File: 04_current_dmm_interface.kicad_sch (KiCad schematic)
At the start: 17 parts, among them J10 POMONA 73099 BLACK, J11 POMONA 73099 RED, J12 POMONA 73099 BLACK, J4 1190370 16POS, J5 691137710006 DMM, J6 POMONA 73099 RED, J8 POMONA 73099 BLACK, J9 POMONA 73099 RED, K13 UD2-5NE, K14 UD2-5NE, K15 UD2-5NE, K16 UD2-5NE

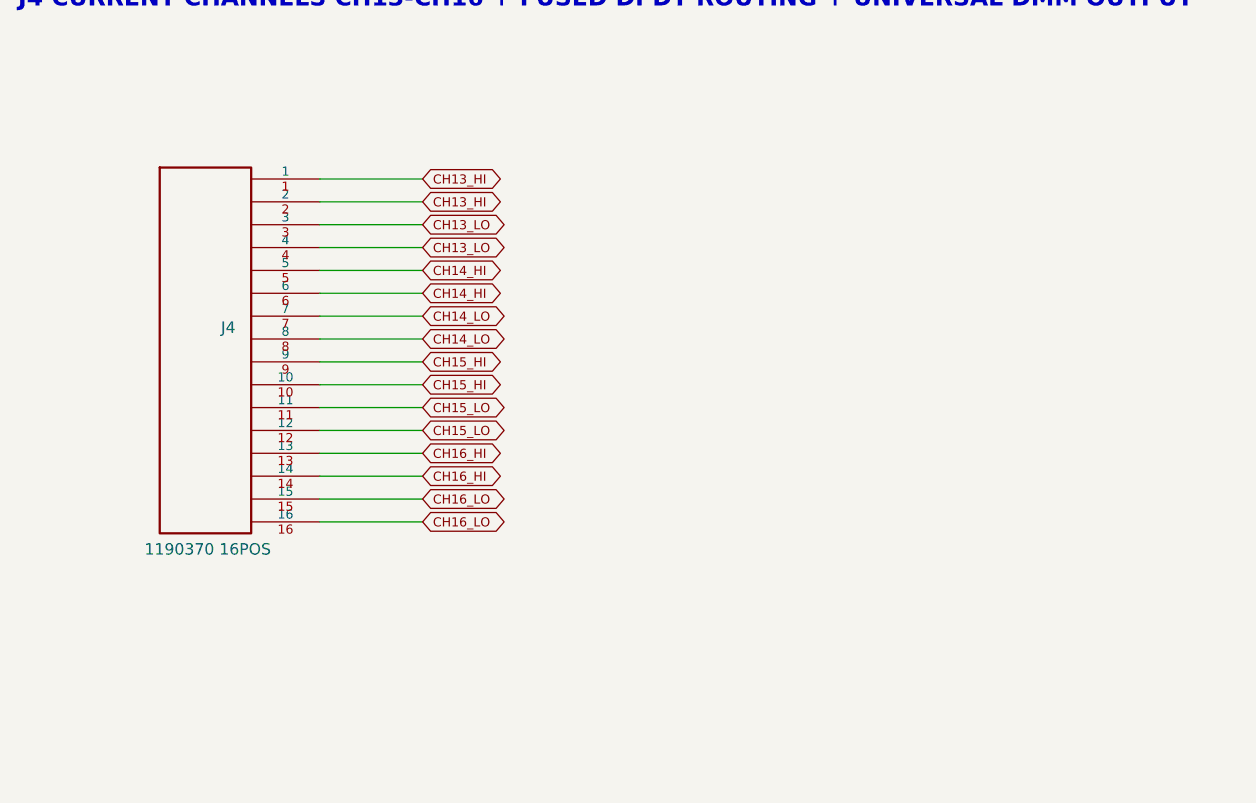
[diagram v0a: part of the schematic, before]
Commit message: Add Phoenix 1190370 connector footprint
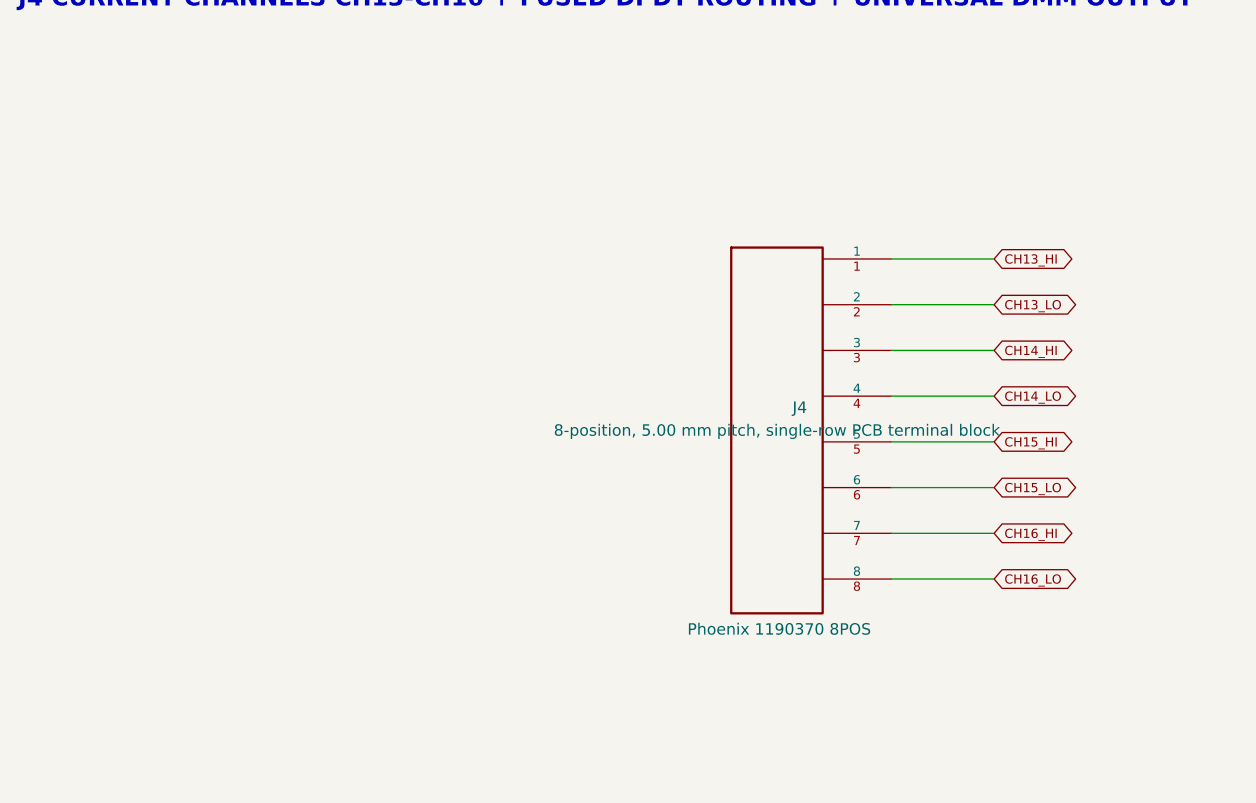
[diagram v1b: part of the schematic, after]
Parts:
- J4: value 1190370 16POS -> Phoenix 1190370 8POS; footprint (none) -> BenchScan_Connectors:Phoenix_1190370_LPTA-2.5-8-5.0; symbol BenchScan_DMMX16-rescue:CONN16 -> BenchScan_DMMX16-rescue:CONN8
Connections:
- net CH13_HI: no longer J4.2
- net CH13_LO: now also J4.2; no longer J4.3, J4.4
- net CH14_HI: now also J4.3; no longer J4.5, J4.6
- net CH14_LO: now also J4.4; no longer J4.7, J4.8
- net CH15_HI: now also J4.5; no longer J4.10, J4.9
- net CH15_LO: now also J4.6; no longer J4.11, J4.12
- net CH16_HI: now also J4.7; no longer J4.13, J4.14
- net CH16_LO: now also J4.8; no longer J4.15, J4.16

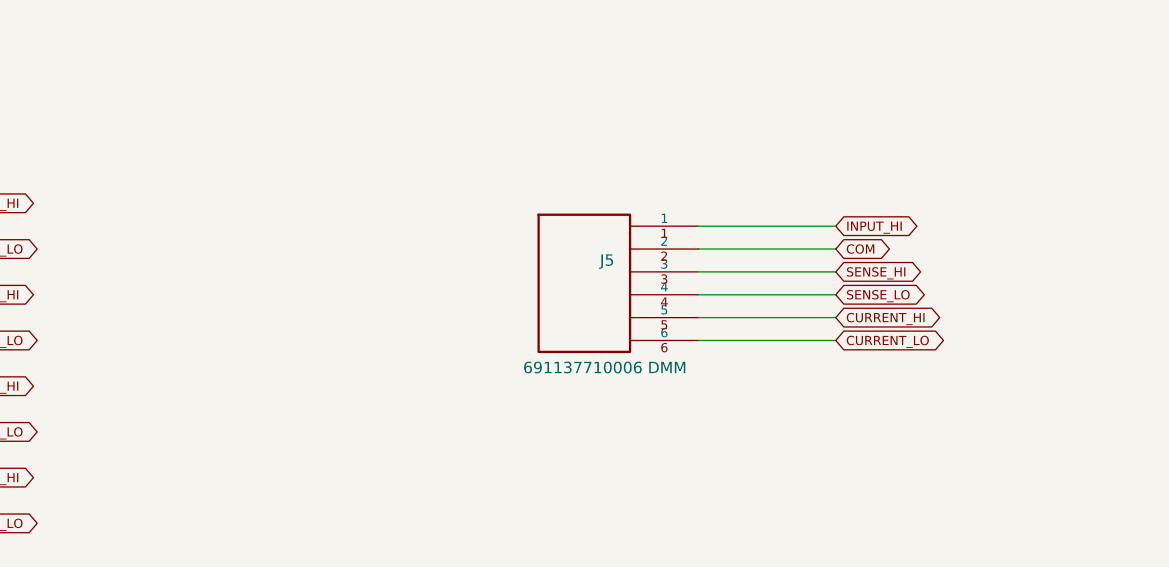
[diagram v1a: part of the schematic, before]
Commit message: Import XIAO and Wurth vendor footprints
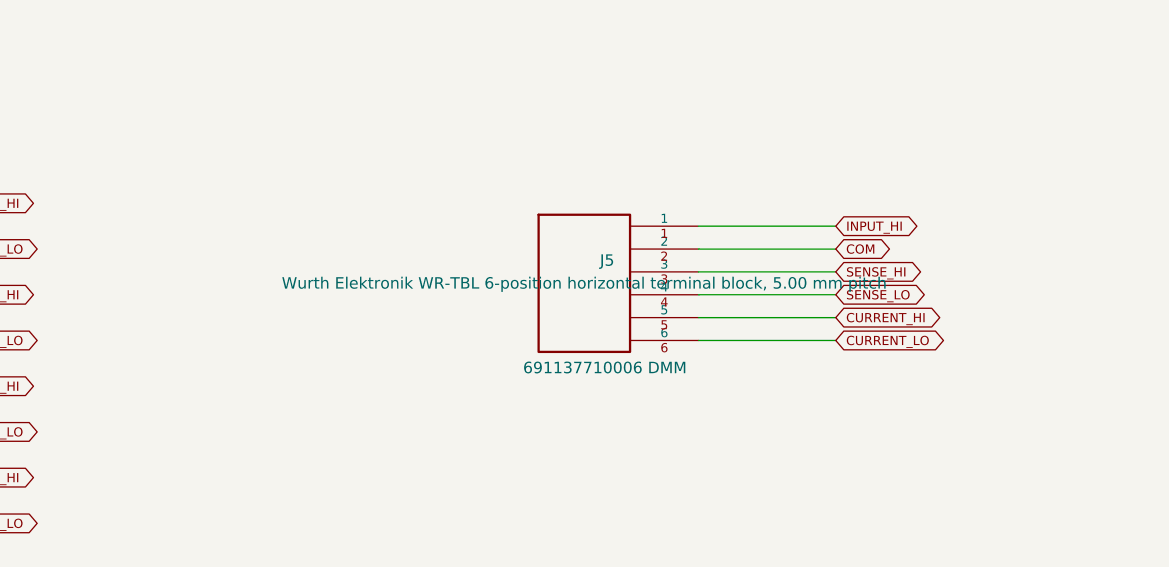
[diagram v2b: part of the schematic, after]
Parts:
- J5: footprint (none) -> Wurth_Connectors:J_Wurth_WR-TBL_691137710006
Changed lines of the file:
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@@
 			)
 		)
-		(property "Footprint" ""
+		(property "Footprint" "Wurth_Connectors:J_Wurth_WR-TBL_691137710006"
 			(at 193.04 54.61 0)
 			(hide yes)
@@
 			)
 		)
-		(property "Datasheet" ""
+		(property "Datasheet" "https://www.we-online.com/components/products/datasheet/691137710006.pdf"
 			(at 193.04 54.61 0)
 			(hide yes)
@@
 			)
 		)
-		(property "Description" ""
+		(property "Description" "Wurth Elektronik WR-TBL 6-position horizontal terminal block, 5.00 mm pitch"
 			(at 193.04 54.61 0)
 			(show_name no)

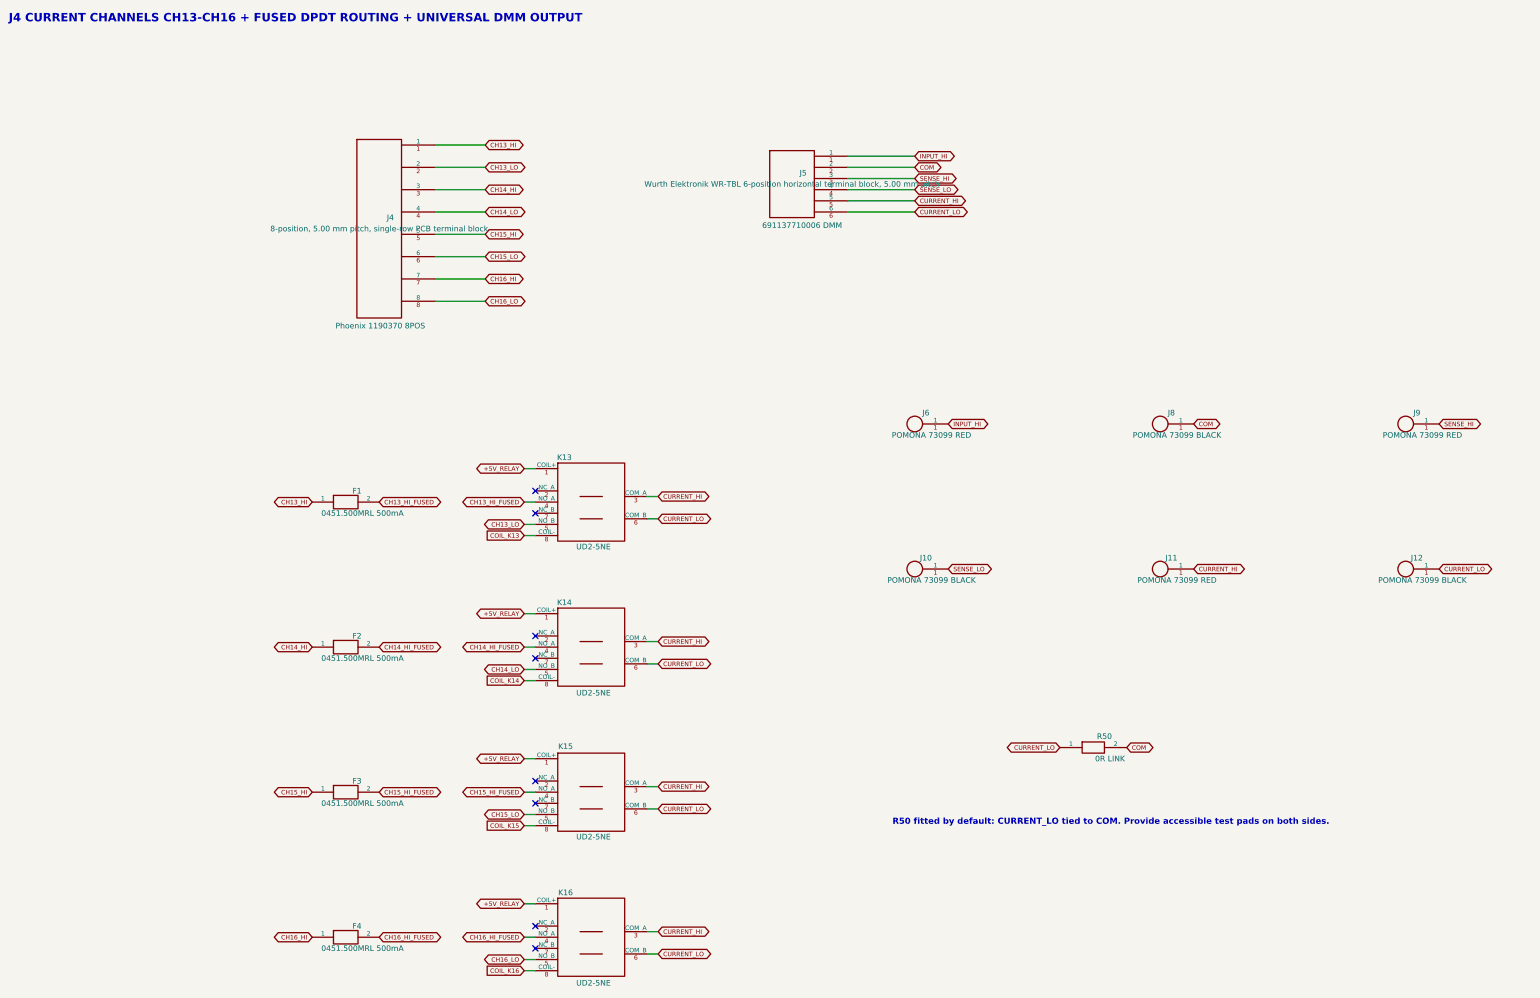
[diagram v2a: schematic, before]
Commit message: Assign custom footprints to schematic components
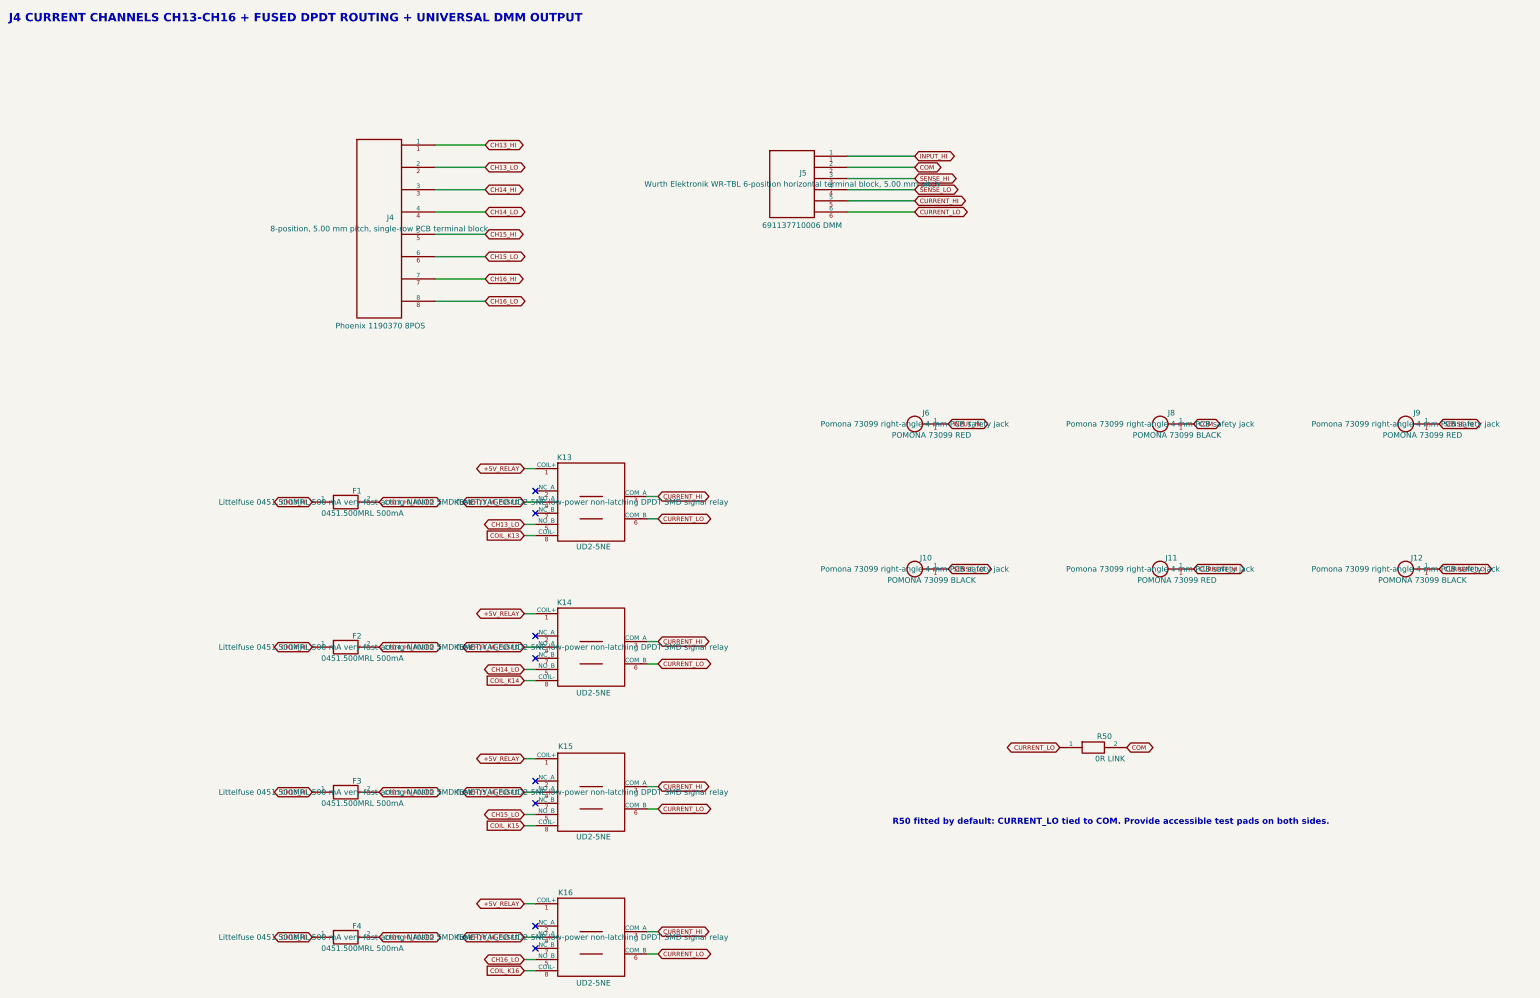
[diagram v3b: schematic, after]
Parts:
- F1, F2, F3, F4: footprint (none) -> BenchScan_Custom:Fuse_Littelfuse_0451_NANO2_2410
- J10, J11, J12, J6, J8, J9: footprint (none) -> BenchScan_Custom:Pomona_73099_RightAngle_SafetyJack
- K13, K14, K15, K16: footprint (none) -> BenchScan_Custom:Relay_KEMET_UD2_NE
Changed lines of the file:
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@@
 			)
 		)
-		(property "Footprint" ""
+		(property "Footprint" "BenchScan_Custom:Fuse_Littelfuse_0451_NANO2_2410"
 			(at 91.44 127 0)
 			(hide yes)
@@
 			)
 		)
-		(property "Datasheet" ""
+		(property "Datasheet" "https://www.littelfuse.com/assetdocs/fuse-451-and-453-datasheet?assetguid=533cd5cc-956c-4243-867f-6ab5a62f6ba1"
 			(at 91.44 127 0)
 			(hide yes)
@@
 			)
 		)
-		(property "Description" ""
+		(property "Description" "Littelfuse 0451.500MRL 500 mA very-fast-acting NANO2 SMD fuse"
 			(at 91.44 127 0)
 			(show_name no)
@@
 			)
 		)
-		(property "Footprint" ""
+		(property "Footprint" "BenchScan_Custom:Fuse_Littelfuse_0451_NANO2_2410"
 			(at 91.44 160.02 0)
 			(hide yes)
@@
 			)
 		)
-		(property "Datasheet" ""
+		(property "Datasheet" "https://www.littelfuse.com/assetdocs/fuse-451-and-453-datasheet?assetguid=533cd5cc-956c-4243-867f-6ab5a62f6ba1"
 			(at 91.44 160.02 0)
 			(hide yes)
@@
 			)
 		)
-		(property "Description" ""
+		(property "Description" "Littelfuse 0451.500MRL 500 mA very-fast-acting NANO2 SMD fuse"
 			(at 91.44 160.02 0)
 			(show_name no)
@@
 			)
 		)
-		(property "Footprint" ""
+		(property "Footprint" "BenchScan_Custom:Fuse_Littelfuse_0451_NANO2_2410"
 			(at 91.44 193.04 0)
 			(hide yes)
@@
 			)
 		)
-		(property "Datasheet" ""
+		(property "Datasheet" "https://www.littelfuse.com/assetdocs/fuse-451-and-453-datasheet?assetguid=533cd5cc-956c-4243-867f-6ab5a62f6ba1"
 			(at 91.44 193.04 0)
 			(hide yes)
@@
 			)
 		)
-		(property "Description" ""
+		(property "Description" "Littelfuse 0451.500MRL 500 mA very-fast-acting NANO2 SMD fuse"
 			(at 91.44 193.04 0)
 			(show_name no)
@@
 			)
 		)
-		(property "Footprint" ""
+		(property "Footprint" "BenchScan_Custom:Fuse_Littelfuse_0451_NANO2_2410"
 			(at 91.44 226.06 0)
 			(hide yes)
@@
 			)
 		)
-		(property "Datasheet" ""
+		(property "Datasheet" "https://www.littelfuse.com/assetdocs/fuse-451-and-453-datasheet?assetguid=533cd5cc-956c-4243-867f-6ab5a62f6ba1"
 			(at 91.44 226.06 0)
 			(hide yes)
@@
 			)
 		)
-		(property "Description" ""
+		(property "Description" "Littelfuse 0451.500MRL 500 mA very-fast-acting NANO2 SMD fuse"
 			(at 91.44 226.06 0)
 			(show_name no)
@@
 			)
 		)
-		(property "Footprint" ""
+		(property "Footprint" "BenchScan_Custom:Relay_KEMET_UD2_NE"
 			(at 147.32 127 0)
 			(hide yes)
@@
 			)
 		)
-		(property "Datasheet" ""
+		(property "Datasheet" "https://content.kemet.com/datasheets/KEM_R7005_UC2_UD2.pdf"
 			(at 147.32 127 0)
 			(hide yes)
@@
 			)
 		)
-		(property "Description" ""
+		(property "Description" "KEMET/YAGEO UD2-5NE low-power non-latching DPDT SMD signal relay"
 			(at 147.32 127 0)
 			(show_name no)
@@
 			)
 		)
-		(property "Footprint" ""
+		(property "Footprint" "BenchScan_Custom:Relay_KEMET_UD2_NE"
 			(at 147.32 160.02 0)
 			(hide yes)
@@
 			)
 		)
-		(property "Datasheet" ""
+		(property "Datasheet" "https://content.kemet.com/datasheets/KEM_R7005_UC2_UD2.pdf"
 			(at 147.32 160.02 0)
 			(hide yes)
@@
 			)
 		)
-		(property "Description" ""
+		(property "Description" "KEMET/YAGEO UD2-5NE low-power non-latching DPDT SMD signal relay"
 			(at 147.32 160.02 0)
 			(show_name no)
@@
 			)
 		)
-		(property "Footprint" ""
+		(property "Footprint" "BenchScan_Custom:Relay_KEMET_UD2_NE"
 			(at 147.32 193.04 0)
 			(hide yes)
@@
 			)
 		)
-		(property "Datasheet" ""
+		(property "Datasheet" "https://content.kemet.com/datasheets/KEM_R7005_UC2_UD2.pdf"
 			(at 147.32 193.04 0)
 			(hide yes)
@@
 			)
 		)
-		(property "Description" ""
+		(property "Description" "KEMET/YAGEO UD2-5NE low-power non-latching DPDT SMD signal relay"
 			(at 147.32 193.04 0)
 			(show_name no)
@@
 			)
 		)
-		(property "Footprint" ""
+		(property "Footprint" "BenchScan_Custom:Relay_KEMET_UD2_NE"
 			(at 147.32 226.06 0)
 			(hide yes)
@@
 			)
 		)
-		(property "Datasheet" ""
+		(property "Datasheet" "https://content.kemet.com/datasheets/KEM_R7005_UC2_UD2.pdf"
 			(at 147.32 226.06 0)
 			(hide yes)
@@
 			)
 		)
-		(property "Description" ""
+		(property "Description" "KEMET/YAGEO UD2-5NE low-power non-latching DPDT SMD signal relay"
 			(at 147.32 226.06 0)
 			(show_name no)
@@
 			)
 		)
-		(property "Footprint" ""
+		(property "Footprint" "BenchScan_Custom:Pomona_73099_RightAngle_SafetyJack"
 			(at 220.98 109.22 0)
 			(hide yes)
@@
 			)
 		)
-		(property "Datasheet" ""
+		(property "Datasheet" "https://www.pomonaelectronics.com/files/datasheets/d73099_101.pdf"
 			(at 220.98 109.22 0)
 			(hide yes)
@@
 			)
 		)
-		(property "Description" ""
+		(property "Description" "Pomona 73099 right-angle 4 mm PCB safety jack"
 			(at 220.98 109.22 0)
 			(show_name no)
@@
 			)
 		)
-		(property "Footprint" ""
+		(property "Footprint" "BenchScan_Custom:Pomona_73099_RightAngle_SafetyJack"
 			(at 276.86 109.22 0)
 			(hide yes)
@@
 			)
 		)
-		(property "Datasheet" ""
+		(property "Datasheet" "https://www.pomonaelectronics.com/files/datasheets/d73099_101.pdf"
 			(at 276.86 109.22 0)
 			(hide yes)
@@
 			)
 		)
-		(property "Description" ""
+		(property "Description" "Pomona 73099 right-angle 4 mm PCB safety jack"
 			(at 276.86 109.22 0)
 			(show_name no)
@@
 			)
 		)
-		(property "Footprint" ""
+		(property "Footprint" "BenchScan_Custom:Pomona_73099_RightAngle_SafetyJack"
 			(at 332.74 109.22 0)
 			(hide yes)
@@
 			)
 		)
-		(property "Datasheet" ""
+		(property "Datasheet" "https://www.pomonaelectronics.com/files/datasheets/d73099_101.pdf"
 			(at 332.74 109.22 0)
 			(hide yes)
@@
 			)
 		)
-		(property "Description" ""
+		(property "Description" "Pomona 73099 right-angle 4 mm PCB safety jack"
 			(at 332.74 109.22 0)
 			(show_name no)
@@
 			)
 		)
-		(property "Footprint" ""
+		(property "Footprint" "BenchScan_Custom:Pomona_73099_RightAngle_SafetyJack"
 			(at 220.98 142.24 0)
 			(hide yes)
@@
 			)
 		)
-		(property "Datasheet" ""
+		(property "Datasheet" "https://www.pomonaelectronics.com/files/datasheets/d73099_101.pdf"
 			(at 220.98 142.24 0)
 			(hide yes)
@@
 			)
 		)
-		(property "Description" ""
+		(property "Description" "Pomona 73099 right-angle 4 mm PCB safety jack"
 			(at 220.98 142.24 0)
 			(show_name no)
@@
 			)
 		)
-		(property "Footprint" ""
+		(property "Footprint" "BenchScan_Custom:Pomona_73099_RightAngle_SafetyJack"
 			(at 276.86 142.24 0)
 			(hide yes)
@@
 			)
 		)
-		(property "Datasheet" ""
+		(property "Datasheet" "https://www.pomonaelectronics.com/files/datasheets/d73099_101.pdf"
 			(at 276.86 142.24 0)
 			(hide yes)
@@
 			)
 		)
-		(property "Description" ""
+		(property "Description" "Pomona 73099 right-angle 4 mm PCB safety jack"
 			(at 276.86 142.24 0)
 			(show_name no)
@@
 			)
 		)
-		(property "Footprint" ""
+		(property "Footprint" "BenchScan_Custom:Pomona_73099_RightAngle_SafetyJack"
 			(at 332.74 142.24 0)
 			(hide yes)
@@
 			)
 		)
-		(property "Datasheet" ""
+		(property "Datasheet" "https://www.pomonaelectronics.com/files/datasheets/d73099_101.pdf"
 			(at 332.74 142.24 0)
 			(hide yes)
@@
 			)
 		)
-		(property "Description" ""
+		(property "Description" "Pomona 73099 right-angle 4 mm PCB safety jack"
 			(at 332.74 142.24 0)
 			(show_name no)
